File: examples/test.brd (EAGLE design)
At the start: 54 x 20.9 mm, 63 parts, among them CON1 MINI-USB_SHIELD5P4-B, IC2 MIC5219-3.3YMM, IC3 74LVC125A, IC4 74LVC126A, IC5 74LVC125A, Q1 12MHz, T1 BC807-25-N, T2 BC817-25-N

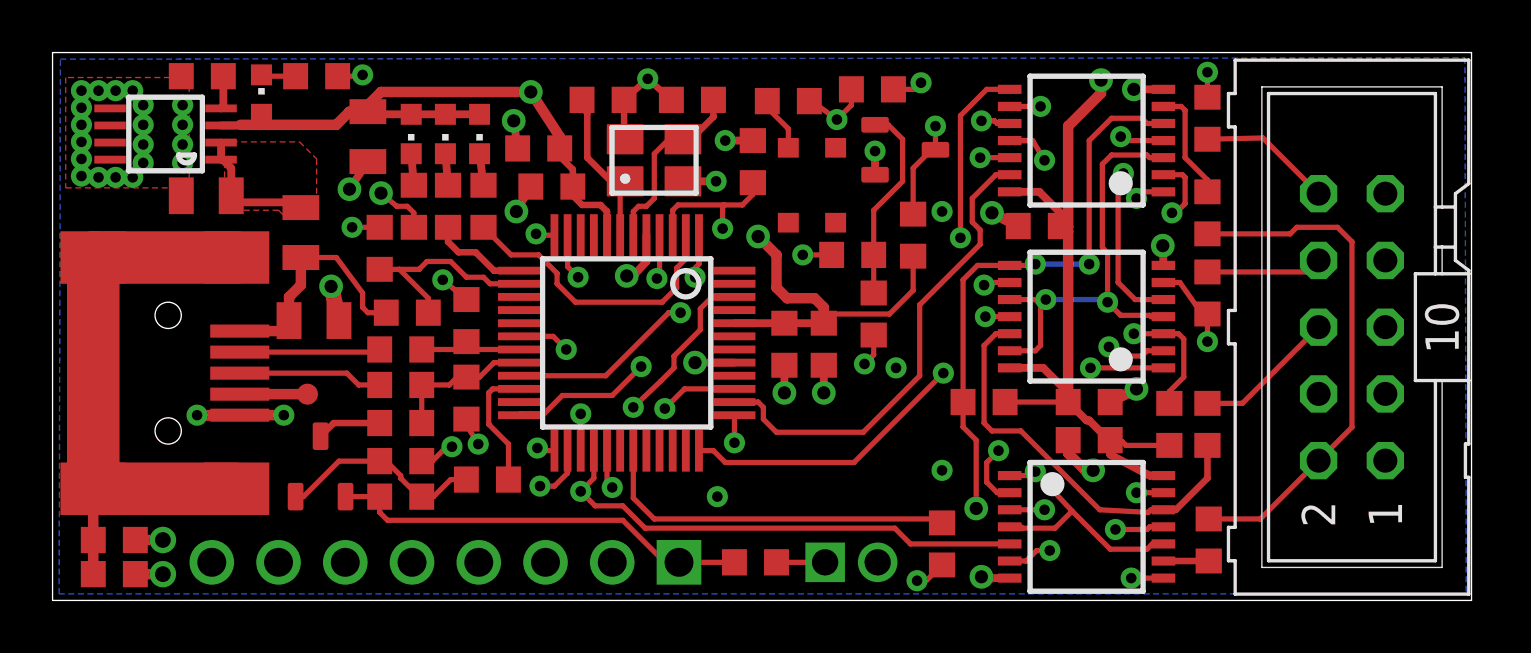
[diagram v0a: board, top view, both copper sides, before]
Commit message: - Added new generated QFP Packages
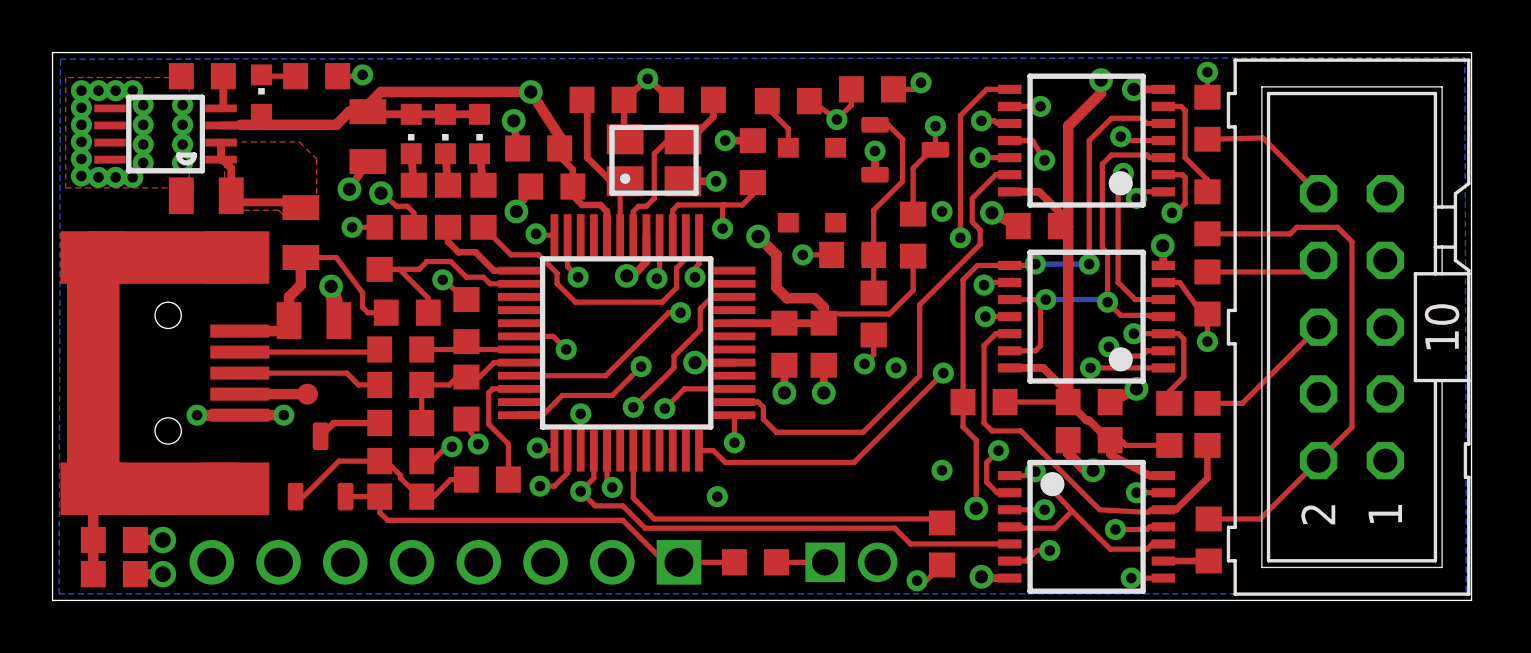
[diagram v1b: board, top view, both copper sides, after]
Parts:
- IC1: device xyz:LQFP48-7X7 -> xyz:QFP50P900X900X160-48N
- turned IC1 to 90 degrees
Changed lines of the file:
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@@
 </autorouter>
 <elements>
-<element name="IC1" library="xyz" package="LQFP48-7X7" value="" x="21.85" y="9.8" smashed="yes" rot="R180"/>
+<element name="IC1" library="xyz" package="QFP50P900X900X160-48N" value="" x="21.85" y="9.8" smashed="yes" rot="R90"/>
 <element name="IC2" library="v-reg-micrel" package="MSOP08" value="MIC5219-3.3YMM" x="4.3" y="17.75" smashed="yes" rot="R90">
 <attribute name="MF" value="" x="4.3" y="17.75" size="1.778" layer="27" rot="R90" display="off"/>
